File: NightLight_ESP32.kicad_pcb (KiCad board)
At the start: 2 copper layers, 38.1 x 43.2 mm, 25 parts, among them J1 USB_OTG, J2 BUTTON, Q1 MMBT2222, Q2 MMBT2222, SW1 TL3342, SW2 TL3342, U1 ESP32-WROOM-32D, U2 AP2112K-3.3, U3 CP2104

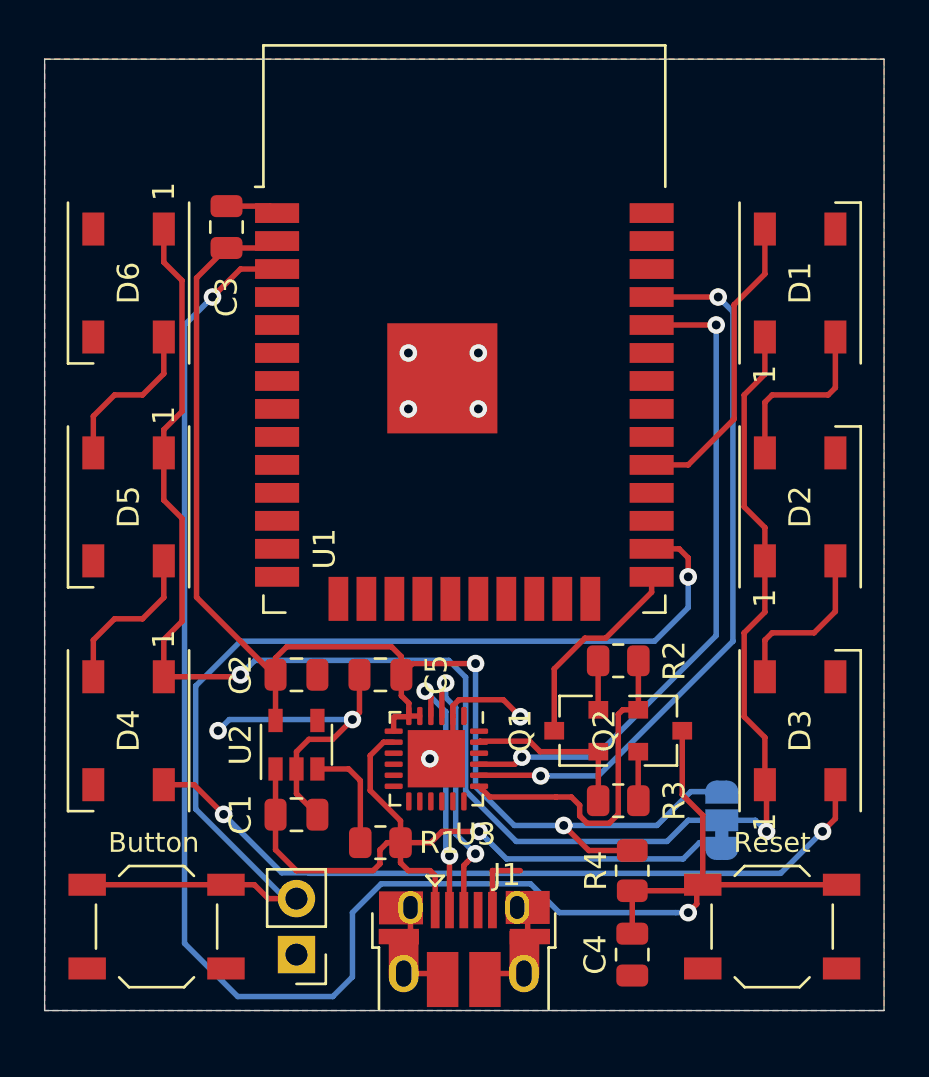
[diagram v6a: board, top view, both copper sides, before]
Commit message: Updated to USB C and CH340
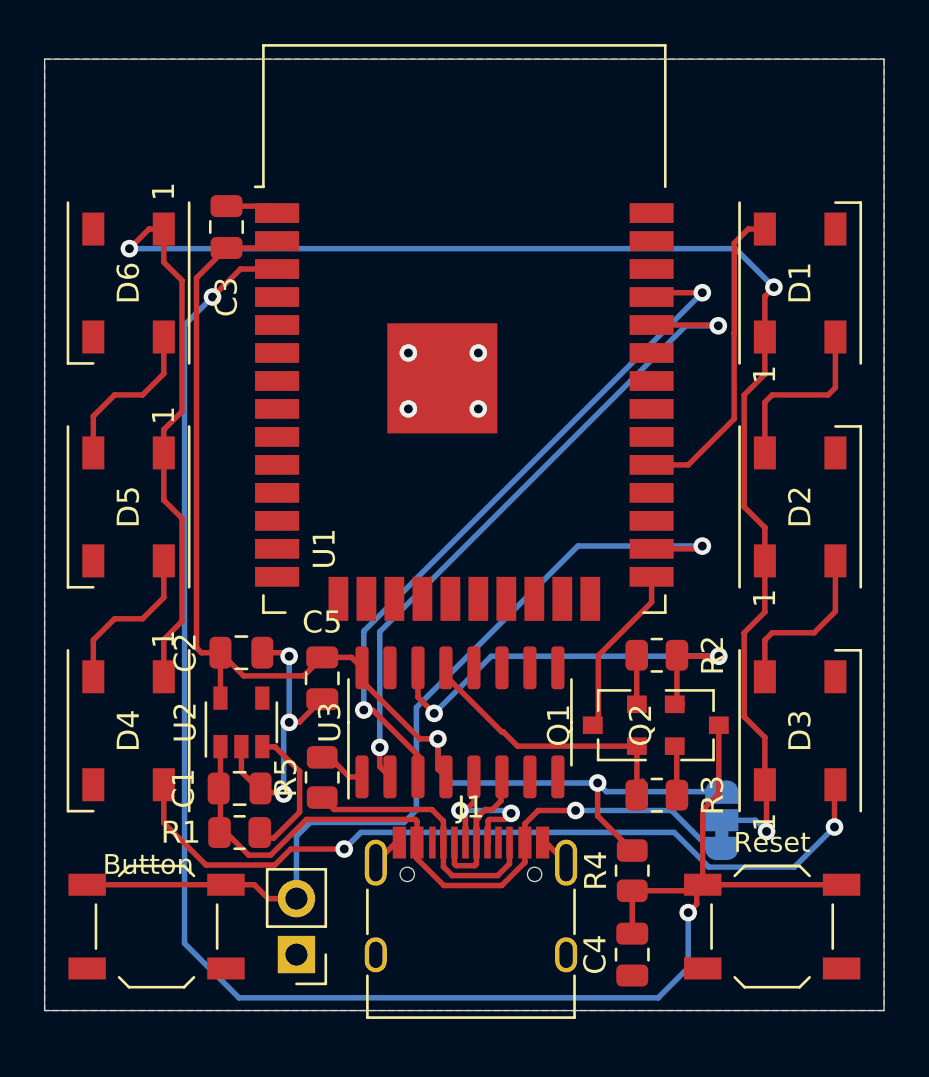
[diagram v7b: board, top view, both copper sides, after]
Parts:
- added R5: 5K1, Resistor_SMD:R_0805_2012Metric, F.Cu at (133.2, 121.5)
- J1: value USB_OTG -> USB_C_Receptacle_USB2.0; footprint Connector_USB:USB_Micro-B_Amphenol_10103594-0001LF_Horizontal -> Connector_USB:USB_C_Receptacle_HRO_TYPE-C-31-M-12
- U3: value CP2104 -> CH340C; footprint Package_DFN_QFN:QFN-24-1EP_4x4mm_P0.5mm_EP2.6x2.6mm -> Package_SO:SOIC-16_3.9x9.9mm_P1.27mm
- moved R1 6.41 mm to (129.5, 124.0), turned to 0 degrees
- moved C1 2.84 mm to (129.5, 122.0)
- moved U2 2.70 mm to (129.6, 119.0)
- moved C2 2.69 mm to (129.6, 115.8)
- moved C5 2.64 mm to (133.2, 117.0), turned to 270 degrees
- moved U3 1.97 mm to (139.5, 119.0), turned to 90 degrees
- moved Q1 1.77 mm to (146.5, 119.1)
- moved R2 1.77 mm to (148.4, 116.0)
- moved R3 1.77 mm to (148.4, 122.3)
- moved Q2 1.68 mm to (150.2, 119.1)
- moved J1 0.84 mm to (140.0, 128.5)
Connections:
- D6 pad 2: Net-(D6-Pad2) -> (no net)
- U1 pad 10: Net-(U1-Pad10) -> (no net)
- U1 pad 11: Net-(U1-Pad11) -> (no net)
- U1 pad 12: Net-(U1-Pad12) -> (no net)
- U1 pad 13: Net-(U1-Pad13) -> (no net)
- U1 pad 14: Net-(U1-Pad14) -> (no net)
- U1 pad 16: Net-(U1-Pad16) -> (no net)
- U1 pad 17: Net-(U1-Pad17) -> (no net)
- U1 pad 18: Net-(U1-Pad18) -> (no net)
- U1 pad 19: Net-(U1-Pad19) -> (no net)
- U1 pad 20: Net-(U1-Pad20) -> (no net)
- U1 pad 21: Net-(U1-Pad21) -> (no net)
- U1 pad 22: Net-(U1-Pad22) -> (no net)
- U1 pad 23: Net-(U1-Pad23) -> (no net)
- U1 pad 24: Net-(U1-Pad24) -> (no net)
- U1 pad 27: Net-(U1-Pad27) -> (no net)
- U1 pad 28: Net-(U1-Pad28) -> (no net)
- U1 pad 30: Net-(U1-Pad30) -> (no net)
- U1 pad 31: Net-(U1-Pad31) -> (no net)
- U1 pad 32: Net-(U1-Pad32) -> (no net)
- U1 pad 33: Net-(U1-Pad33) -> (no net)
- U1 pad 36: Net-(U1-Pad36) -> (no net)
- U1 pad 37: Net-(U1-Pad37) -> (no net)
- U1 pad 4: Net-(U1-Pad4) -> (no net)
- U1 pad 5: Net-(U1-Pad5) -> (no net)
- U1 pad 6: Net-(U1-Pad6) -> (no net)
- U1 pad 7: Net-(U1-Pad7) -> (no net)
- U1 pad 8: Net-(U1-Pad8) -> (no net)
- U1 pad 9: Net-(U1-Pad9) -> (no net)
- U2 pad 4: Net-(U2-Pad4) -> (no net)
- U3 pad 1: Net-(U3-Pad1) -> GND
- U3 pad 10: Net-(U3-Pad10) -> (no net)
- U3 pad 11: Net-(U3-Pad11) -> (no net)
- U3 pad 12: Net-(U3-Pad12) -> (no net)
- U3 pad 13: Net-(U3-Pad13) -> /DTR
- U3 pad 14: Net-(U3-Pad14) -> /RTS
- U3 pad 15: Net-(U3-Pad15) -> (no net)
- U3 pad 16: Net-(U3-Pad16) -> +3V3
- U3 pad 2: GND -> /RXD0
- U3 pad 3: /D+ -> /TXD0
- U3 pad 4: /D- -> +3V3
- U3 pad 5: +3V3 -> /D+
- U3 pad 6: +3V3 -> /D-
- U3 pad 7: +3V3 -> (no net)
- U3 pad 8: VBUS -> (no net)
- U3 pad 9: Net-(U3-Pad9) -> (no net)
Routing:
- net GND: track 49.9 -> 30.4 mm, vias 8 -> 7
- net Net-(J1-PadA5): track 0.00 -> 12.4 mm
- net /BUTTON: track 49.5 -> 41.5 mm
- net +3V3: track 63.1 -> 57.6 mm
- net /RTS: track 15.2 -> 20.3 mm, vias 0 -> 2
- net /DTR: track 7.22 -> 12.2 mm
- net /D+: track 12.9 -> 7.95 mm
- net /D-: track 11.9 -> 7.14 mm, vias 2 -> 0
- net VBUS: track 36.5 -> 33.0 mm
- net Net-(D3-Pad2): track 34.7 -> 36.9 mm
- net /LED_POWER: track 80.4 -> 82.3 mm, vias 2 -> 3
- net /GPIO0: track 9.37 -> 7.74 mm
- net Net-(R1-Pad2): track 4.98 -> 6.31 mm
- net /RESET: track 81.6 -> 80.5 mm
- net /TXD0: track 33.0 -> 32.0 mm
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
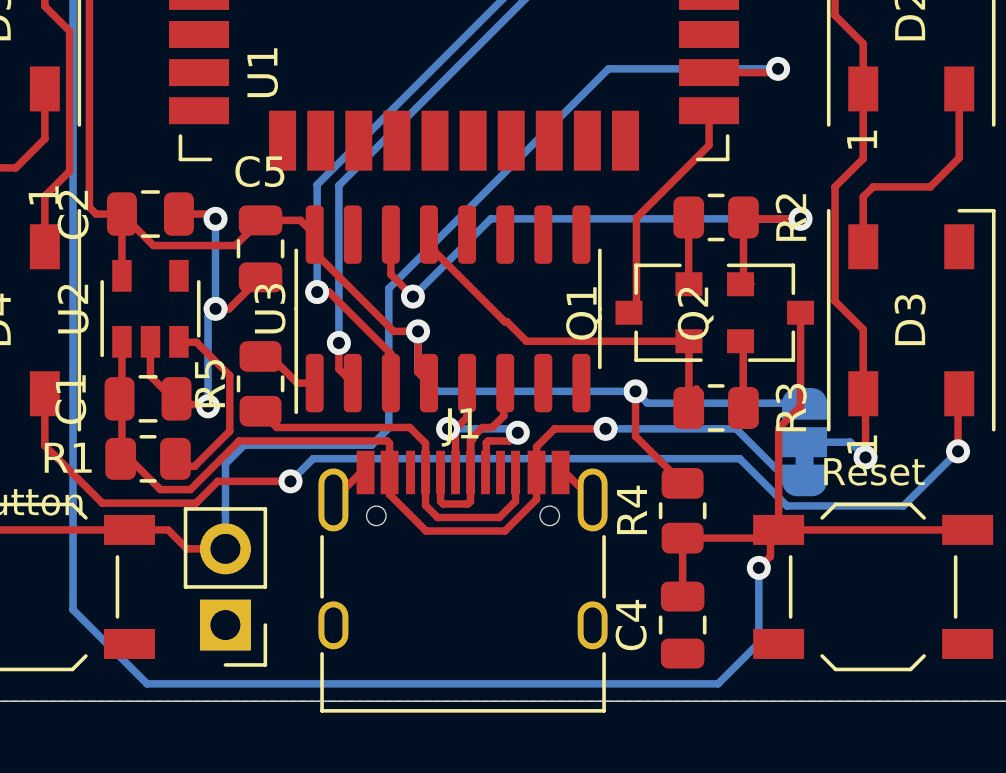
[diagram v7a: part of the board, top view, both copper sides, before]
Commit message: Fix issue with USB C CC1/CC2 needing two resistors and the wrong schematic symbol for the MMBT2222, leading to the wrong pinout
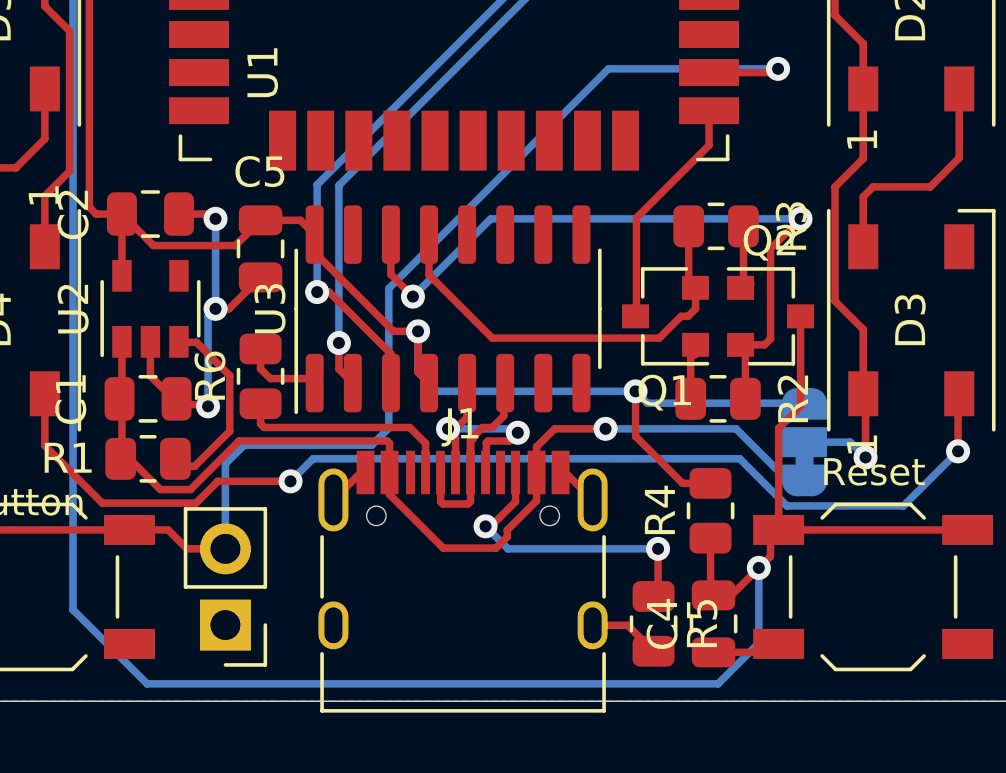
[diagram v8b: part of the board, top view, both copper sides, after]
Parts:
- added R6: 5K1, Resistor_SMD:R_0805_2012Metric, F.Cu at (133.2, 121.2)
- moved R5 15.3 mm to (146.3, 129.5), turned to 270 degrees
- moved R3 6.06 mm to (148.4, 116.2)
- moved R2 6.05 mm to (148.5, 122.0)
- moved C4 1.03 mm to (148.3, 129.5)
- moved R4 0.93 mm to (148.2, 125.7)
- moved Q1 0.25 mm to (146.8, 119.2)
- moved Q2 0.12 mm to (150.2, 119.2)
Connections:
- J1 pad B5: Net-(J1-PadA5) -> Net-(J1-PadB5)
- Q1 pad 1: /DTR -> Net-(Q1-Pad1)
- Q1 pad 2: Net-(Q1-Pad2) -> /DTR
- Q2 pad 1: /RTS -> Net-(Q2-Pad1)
- Q2 pad 2: Net-(Q2-Pad2) -> /RTS
- R2 pad 1: Net-(Q1-Pad2) -> Net-(Q1-Pad1)
- R3 pad 1: Net-(Q2-Pad2) -> Net-(Q2-Pad1)
- R5 pad 1: Net-(J1-PadA5) -> Net-(J1-PadB5)
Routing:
- net Net-(J1-PadB5): track 0.00 -> 9.96 mm, vias 0 -> 2
- net Net-(J1-PadA5): track 12.4 -> 7.16 mm
- net GND: track 30.4 -> 35.3 mm
- net /RTS: track 20.3 -> 23.7 mm
- net Net-(Q2-Pad1): track 0.00 -> 2.29 mm
- net Net-(Q2-Pad2): track 2.23 -> 0.00 mm
- net Net-(Q1-Pad1): track 0.00 -> 1.63 mm
- net /DTR: track 12.2 -> 13.8 mm
- net Net-(Q1-Pad2): track 1.59 -> 0.00 mm
- net /RESET: track 80.5 -> 79.5 mm
- net VBUS: track 33.0 -> 33.6 mm
- net +3V3: track 57.6 -> 58.2 mm
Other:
- board text added: "v1.2"
- board text removed: "v1.1"
